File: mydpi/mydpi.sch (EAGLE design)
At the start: 34 parts, among them Q1 DMN3404L, U1 MEGA32U4-MU, U2 RT9193-33GB, Y1 830069392

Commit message: Bugfixes in used libraries
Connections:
- removed net MEDBG_UPDI: DBG1.UDPI, R4.2
- new net N$3: R4.2
- new net UDPI: DBG1.UDPI
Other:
- note added: "ATmega32U4 ICSP"
- note added: "ATmega32u4"
- note added: "Crystal Circuit"
- note added: "Decoupling Capacitors"
- note added: "Reset Circuit"
- note added: "Supply LED"
- note added: "Target Voltage Level Shifter"
- note added: "Target Voltage Selection"
- note added: "UDPI Programming Connector Wurth Electronics SKEDD"
- note added: "USB C Connector"
- moved on the sheet: C1, C10, C11, C12, C13, C14, C2, C3, C4, C5, C7, C8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

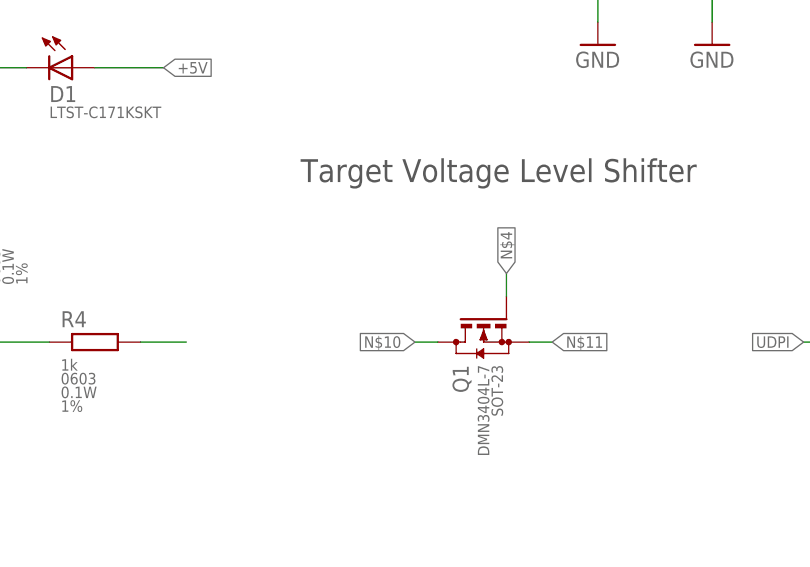
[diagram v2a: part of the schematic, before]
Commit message: Finished level shifter
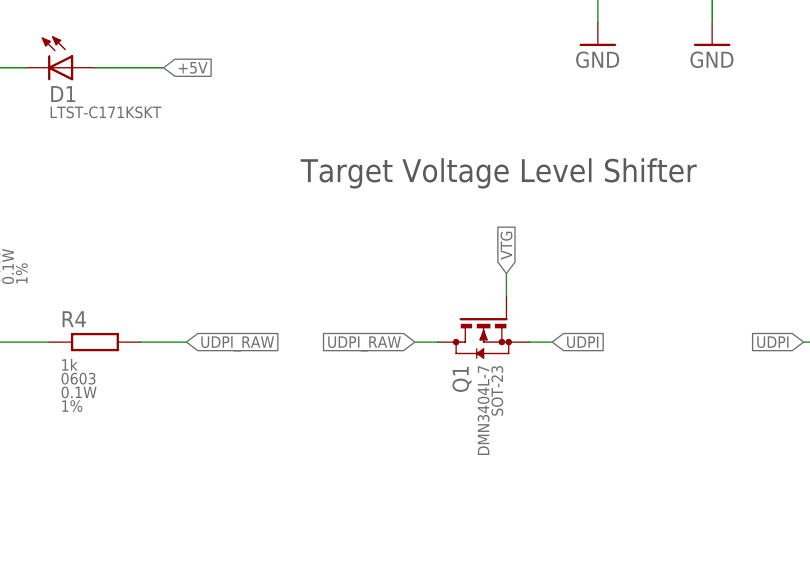
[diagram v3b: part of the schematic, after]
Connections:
- removed net N$10: Q1.D
- removed net N$11: Q1.S
- removed net N$3: R4.2
- removed net N$4: Q1.G
- new net UDPI_RAW: Q1.D, R4.2
- net UDPI: now also Q1.S
- net VTG: now also Q1.G
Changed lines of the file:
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@@
 </segment>
 </net>
-<net name="N$4" class="0">
-<segment>
-<pinref part="Q1" gate="G$1" pin="G"/>
-<wire x1="256.54" y1="152.4" x2="256.54" y2="154.94" width="0.1524" layer="91"/>
-<label x="256.54" y="154.94" size="1.27" layer="95" rot="R90" xref="yes"/>
-</segment>
-</net>
-<net name="N$10" class="0">
+<net name="UDPI_RAW" class="0">
 <segment>
 <pinref part="Q1" gate="G$1" pin="D"/>
@@
 <label x="246.38" y="147.32" size="1.27" layer="95" rot="R180" xref="yes"/>
 </segment>
-</net>
-<net name="N$11" class="0">
 <segment>
-<pinref part="Q1" gate="G$1" pin="S"/>
-<wire x1="259.08" y1="147.32" x2="261.62" y2="147.32" width="0.1524" layer="91"/>
-<label x="261.62" y="147.32" size="1.27" layer="95" xref="yes"/>
+<pinref part="R4" gate="G$1" pin="2"/>
+<wire x1="215.9" y1="147.32" x2="220.98" y2="147.32" width="0.1524" layer="91"/>
+<label x="220.98" y="147.32" size="1.27" layer="95" xref="yes"/>
 </segment>
 </net>
@@
 <label x="309.88" y="104.14" size="1.27" layer="95" xref="yes"/>
 </segment>
+<segment>
+<pinref part="Q1" gate="G$1" pin="G"/>
+<wire x1="256.54" y1="152.4" x2="256.54" y2="154.94" width="0.1524" layer="91"/>
+<label x="256.54" y="154.94" size="1.27" layer="95" rot="R90" xref="yes"/>
+</segment>
 </net>
 <net name="UDPI" class="0">
@@
 <label x="289.56" y="147.32" size="1.27" layer="95" rot="R180" xref="yes"/>
 </segment>
-</net>
-<net name="N$3" class="0">
 <segment>
-<pinref part="R4" gate="G$1" pin="2"/>
-<wire x1="215.9" y1="147.32" x2="220.98" y2="147.32" width="0.1524" layer="91"/>
+<pinref part="Q1" gate="G$1" pin="S"/>
+<wire x1="259.08" y1="147.32" x2="261.62" y2="147.32" width="0.1524" layer="91"/>
+<label x="261.62" y="147.32" size="1.27" layer="95" xref="yes"/>
 </segment>
 </net>

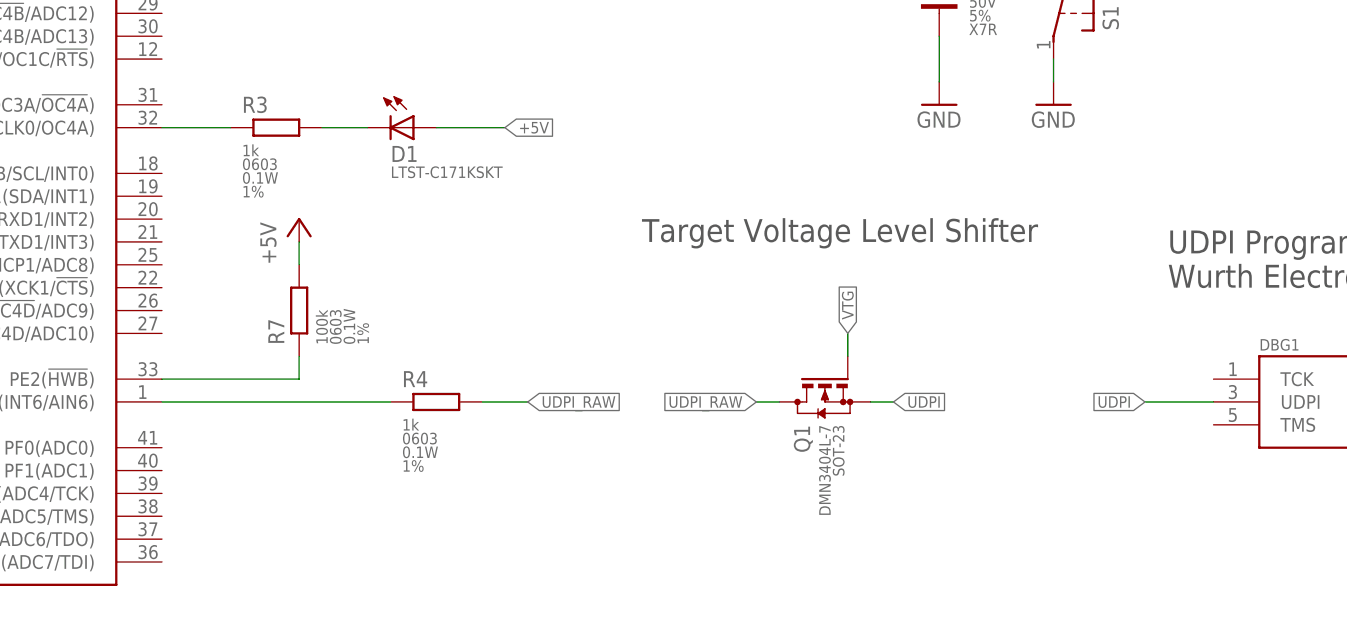
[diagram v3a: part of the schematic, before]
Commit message: Added pullup resistors for level shifting
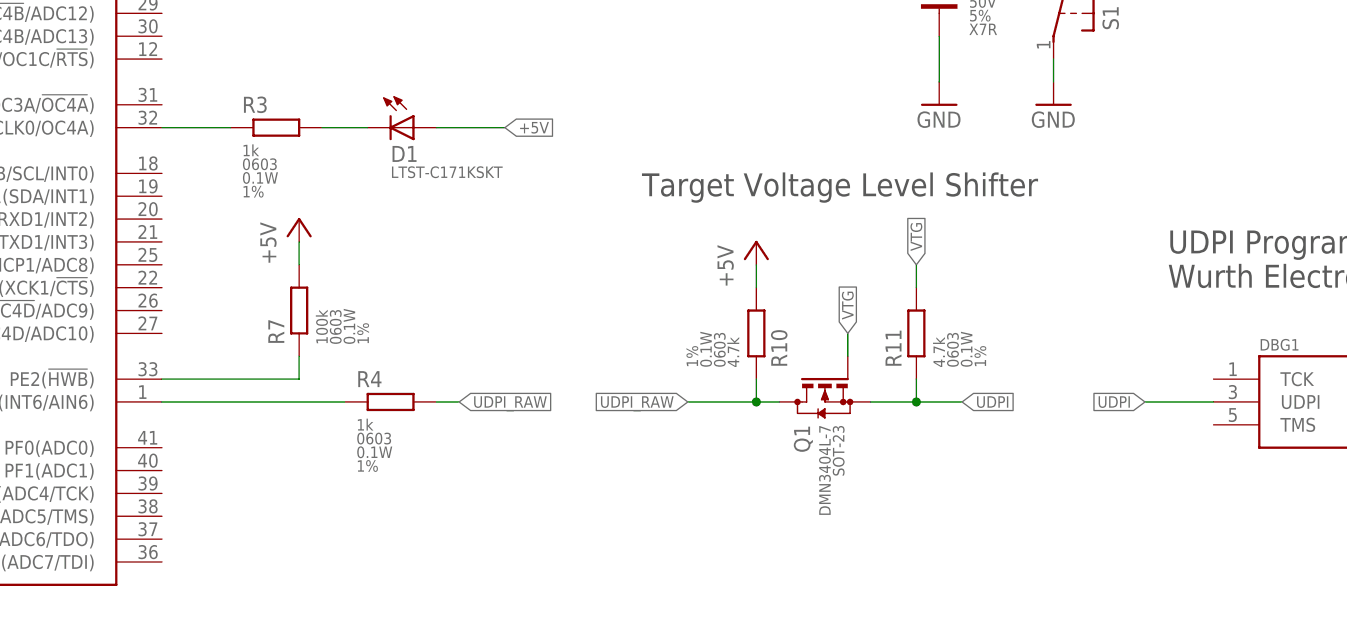
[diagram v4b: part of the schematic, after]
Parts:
- added R10, R11: 4.7k, zaan-Resistors:4.7KOHM-0603-1/10W-1%
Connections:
- net +5V: now also R10.2
- net UDPI: now also R11.1
- net UDPI_RAW: now also R10.1
- net VTG: now also R11.2
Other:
- moved on the sheet: R4
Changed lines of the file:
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@@
 <attribute name="CHECKED_BY" value="-"/>
 <attribute name="DRAWN_BY" value="zaan"/>
-<attribute name="REV" value="1.0"/>
+<attribute name="REV" value="1.1"/>
 <attribute name="TITLE" value="myDPI"/>
 </attributes>
@@
 <part name="P+11" library="supply1" library_urn="urn:adsk.eagle:library:371" deviceset="+5V" device=""/>
 <part name="GND22" library="supply1" library_urn="urn:adsk.eagle:library:371" deviceset="GND" device=""/>
+<part name="R10" library="zaan-Resistors" library_urn="urn:adsk.eagle:library:16759442" deviceset="4.7KOHM" device="-0603-1/10W-1%" package3d_urn="urn:adsk.eagle:package:16759452/1" value="4.7k"/>
+<part name="R11" library="zaan-Resistors" library_urn="urn:adsk.eagle:library:16759442" deviceset="4.7KOHM" device="-0603-1/10W-1%" package3d_urn="urn:adsk.eagle:package:16759452/1" value="4.7k"/>
+<part name="P+8" library="supply1" library_urn="urn:adsk.eagle:library:371" deviceset="+5V" device=""/>
 </parts>
 <sheets>
@@
 <text x="292.1" y="160.02" size="2.54" layer="97">UDPI Programming Connector
 Wurth Electronics SKEDD</text>
-<text x="233.68" y="165.1" size="2.54" layer="97">Target Voltage Level Shifter</text>
+<text x="233.68" y="170.18" size="2.54" layer="97">Target Voltage Level Shifter</text>
 <text x="124.46" y="215.9" size="3.81" layer="97">ATmega32u4</text>
 <text x="73.66" y="104.14" size="2.54" layer="97">Crystal Circuit</text>
@@
 <attribute name="VALUE" x="93.98" y="66.04" size="1.778" layer="96"/>
 </instance>
-<instance part="R4" gate="G$1" x="210.82" y="147.32" smashed="yes">
-<attribute name="NAME" x="207.01" y="149.86" size="1.778" layer="95" align="center-left"/>
-<attribute name="VALUE" x="207.01" y="144.78" size="1.27" layer="96" align="center-left"/>
-<attribute name="PACKAGE-IN" x="207.01" y="143.256" size="1.27" layer="96" align="center-left"/>
-<attribute name="POWER" x="207.01" y="141.732" size="1.27" layer="96" align="center-left"/>
-<attribute name="TOLERANCE" x="207.01" y="140.208" size="1.27" layer="96" align="center-left"/>
+<instance part="R4" gate="G$1" x="205.74" y="147.32" smashed="yes">
+<attribute name="NAME" x="201.93" y="149.86" size="1.778" layer="95" align="center-left"/>
+<attribute name="VALUE" x="201.93" y="144.78" size="1.27" layer="96" align="center-left"/>
+<attribute name="PACKAGE-IN" x="201.93" y="143.256" size="1.27" layer="96" align="center-left"/>
+<attribute name="POWER" x="201.93" y="141.732" size="1.27" layer="96" align="center-left"/>
+<attribute name="TOLERANCE" x="201.93" y="140.208" size="1.27" layer="96" align="center-left"/>
 </instance>
 <instance part="S1" gate="G$1" x="279.4" y="190.5" smashed="yes" rot="MR90">
@@
 <instance part="GND22" gate="1" x="60.96" y="160.02" smashed="yes">
 <attribute name="VALUE" x="58.42" y="157.48" size="1.778" layer="96"/>
+</instance>
+<instance part="R10" gate="G$1" x="246.38" y="154.94" smashed="yes" rot="MR90">
+<attribute name="NAME" x="248.92" y="151.13" size="1.778" layer="95" rot="MR90" align="center-left"/>
+<attribute name="VALUE" x="243.84" y="151.13" size="1.27" layer="96" rot="MR90" align="center-left"/>
+<attribute name="PACKAGE-IN" x="242.316" y="151.13" size="1.27" layer="96" rot="MR90" align="center-left"/>
+<attribute name="POWER" x="240.792" y="151.13" size="1.27" layer="96" rot="MR90" align="center-left"/>
+<attribute name="TOLERANCE" x="239.268" y="151.13" size="1.27" layer="96" rot="MR90" align="center-left"/>
+</instance>
+<instance part="R11" gate="G$1" x="264.16" y="154.94" smashed="yes" rot="R90">
+<attribute name="NAME" x="261.62" y="151.13" size="1.778" layer="95" rot="R90" align="center-left"/>
+<attribute name="VALUE" x="266.7" y="151.13" size="1.27" layer="96" rot="R90" align="center-left"/>
+<attribute name="PACKAGE-IN" x="268.224" y="151.13" size="1.27" layer="96" rot="R90" align="center-left"/>
+<attribute name="POWER" x="269.748" y="151.13" size="1.27" layer="96" rot="R90" align="center-left"/>
+<attribute name="TOLERANCE" x="271.272" y="151.13" size="1.27" layer="96" rot="R90" align="center-left"/>
+</instance>
+<instance part="P+8" gate="1" x="246.38" y="165.1" smashed="yes">
+<attribute name="VALUE" x="243.84" y="160.02" size="1.778" layer="96" rot="R90"/>
 </instance>
 </instances>
@@
 <wire x1="60.96" y1="175.26" x2="60.96" y2="172.72" width="0.1524" layer="91"/>
 </segment>
+<segment>
+<pinref part="R10" gate="G$1" pin="2"/>
+<pinref part="P+8" gate="1" pin="+5V"/>
+<wire x1="246.38" y1="162.56" x2="246.38" y2="160.02" width="0.1524" layer="91"/>
+</segment>
 </net>
 <net name="USB_P" class="1">
@@
 <pinref part="U1" gate="G$1" pin="PE6(INT6/AIN6)"/>
 <pinref part="R4" gate="G$1" pin="1"/>
-<wire x1="180.34" y1="147.32" x2="205.74" y2="147.32" width="0.1524" layer="91"/>
+<wire x1="180.34" y1="147.32" x2="200.66" y2="147.32" width="0.1524" layer="91"/>
 </segment>
 </net>
@@
 <pinref part="Q1" gate="G$1" pin="D"/>
 <wire x1="248.92" y1="147.32" x2="246.38" y2="147.32" width="0.1524" layer="91"/>
-<label x="246.38" y="147.32" size="1.27" layer="95" rot="R180" xref="yes"/>
+<label x="238.76" y="147.32" size="1.27" layer="95" rot="R180" xref="yes"/>
+<pinref part="R10" gate="G$1" pin="1"/>
+<wire x1="246.38" y1="147.32" x2="238.76" y2="147.32" width="0.1524" layer="91"/>
+<wire x1="246.38" y1="149.86" x2="246.38" y2="147.32" width="0.1524" layer="91"/>
+<junction x="246.38" y="147.32"/>
 </segment>
 <segment>
 <pinref part="R4" gate="G$1" pin="2"/>
-<wire x1="215.9" y1="147.32" x2="220.98" y2="147.32" width="0.1524" layer="91"/>
-<label x="220.98" y="147.32" size="1.27" layer="95" xref="yes"/>
+<wire x1="210.82" y1="147.32" x2="213.36" y2="147.32" width="0.1524" layer="91"/>
+<label x="213.36" y="147.32" size="1.27" layer="95" xref="yes"/>
 </segment>
 </net>
@@
 <label x="256.54" y="154.94" size="1.27" layer="95" rot="R90" xref="yes"/>
 </segment>
+<segment>
+<pinref part="R11" gate="G$1" pin="2"/>
+<wire x1="264.16" y1="160.02" x2="264.16" y2="162.56" width="0.1524" layer="91"/>
+<label x="264.16" y="162.56" size="1.27" layer="95" rot="R90" xref="yes"/>
+</segment>
 </net>
 <net name="UDPI" class="0">
@@
 <segment>
 <pinref part="Q1" gate="G$1" pin="S"/>
-<wire x1="259.08" y1="147.32" x2="261.62" y2="147.32" width="0.1524" layer="91"/>
-<label x="261.62" y="147.32" size="1.27" layer="95" xref="yes"/>
-</segment>
-</net>
+<wire x1="259.08" y1="147.32" x2="264.16" y2="147.32" width="0.1524" layer="91"/>
+<label x="269.24" y="147.32" size="1.27" layer="95" xref="yes"/>
+<pinref part="R11" gate="G$1" pin="1"/>
+<wire x1="264.16" y1="147.32" x2="269.24" y2="147.32" width="0.1524" layer="91"/>
+<wire x1="264.16" y1="149.86" x2="264.16" y2="147.32" width="0.1524" layer="91"/>
+<junction x="264.16" y="147.32"/>
+</segment>
+</net>
